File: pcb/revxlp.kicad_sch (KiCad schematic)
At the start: 137 parts, among them Q1 AO3416 N-channel MOSFET, SW1 SW_SPDT, SW2 SW_Push, U1 74HC595, U2 SeeeduinoXIAO_BLE

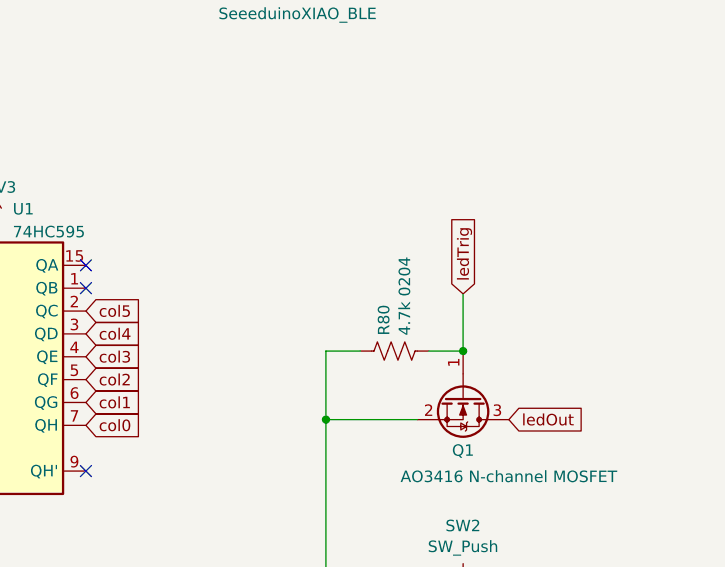
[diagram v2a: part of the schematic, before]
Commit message: Add more LCSC part numbers.
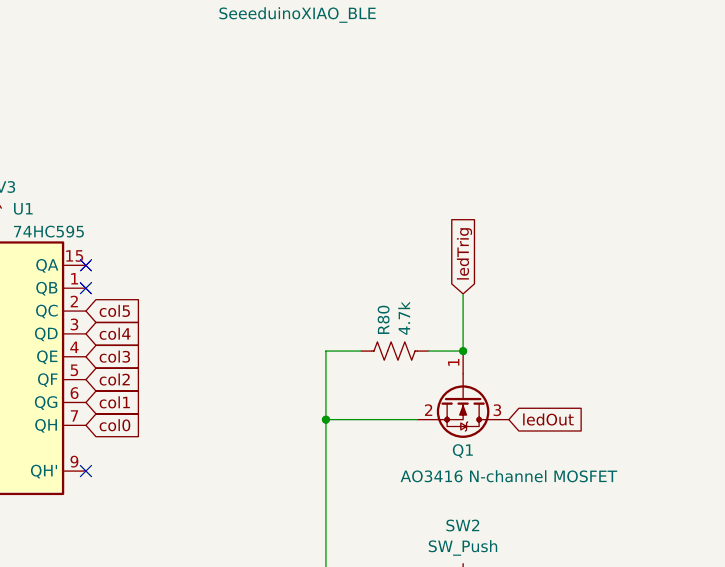
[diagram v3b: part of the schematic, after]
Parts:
- D_A0, D_A1, D_A2, D_A3, D_A4, D_A5, D_B0, D_B1, D_B2, D_B3, D_B4, D_B5, D_C0, D_C1, D_C2, D_C3, D_C4, D_C5, D_D0, D_D1, D_D2, D_D3, D_D4, D_D5, D_E0, D_E1, D_E2, D_E3, D_E4, D_E5, D_F0, D_F1, D_F2, D_F3, D_F4, D_F5, D_G0, D_G1, D_G2, D_G3, D_G4, D_G5: lcsc part number (none) -> C81598
- R80: value 4.7k 0204 -> 4.7k
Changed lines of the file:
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@@
+      (effects (font (size 1.27 1.27)) hide)
+    )
+    (property "lcsc part number" "C81598" (id 4) (at 34.29 39.37 90)
       (effects (font (size 1.27 1.27)) hide)
     )
@@
       (effects (font (size 1.27 1.27)) hide)
     )
+    (property "lcsc part number" "C81598" (id 4) (at 34.29 39.37 90)
+      (effects (font (size 1.27 1.27)) hide)
+    )
     (pin "1")
     (pin "2")
@@
       (effects (font (size 1.27 1.27)) hide)
     )
+    (property "lcsc part number" "C81598" (id 4) (at 34.29 39.37 90)
+      (effects (font (size 1.27 1.27)) hide)
+    )
     (pin "1")
     (pin "2")
@@
       (effects (font (size 1.27 1.27)) hide)
     )
+    (property "lcsc part number" "C81598" (id 4) (at 34.29 39.37 90)
+      (effects (font (size 1.27 1.27)) hide)
+    )
     (pin "1")
     (pin "2")
@@
       (effects (font (size 1.27 1.27)) hide)
     )
+    (property "lcsc part number" "C81598" (id 4) (at 34.29 39.37 90)
+      (effects (font (size 1.27 1.27)) hide)
+    )
     (pin "1")
     (pin "2")
@@
       (effects (font (size 1.27 1.27)) hide)
     )
+    (property "lcsc part number" "C81598" (id 4) (at 34.29 39.37 90)
+      (effects (font (size 1.27 1.27)) hide)
+    )
     (pin "1")
     (pin "2")
@@
       (effects (font (size 1.27 1.27)) hide)
     )
+    (property "lcsc part number" "C81598" (id 4) (at 34.29 39.37 90)
+      (effects (font (size 1.27 1.27)) hide)
+    )
     (pin "1")
     (pin "2")
@@
       (effects (font (size 1.27 1.27)) hide)
     )
+    (property "lcsc part number" "C81598" (id 4) (at 34.29 39.37 90)
+      (effects (font (size 1.27 1.27)) hide)
+    )
     (pin "1")
     (pin "2")
@@
       (effects (font (size 1.27 1.27)) hide)
     )
+    (property "lcsc part number" "C81598" (id 4) (at 34.29 39.37 90)
+      (effects (font (size 1.27 1.27)) hide)
+    )
     (pin "1")
     (pin "2")
@@
       (effects (font (size 1.27 1.27)) hide)
     )
+    (property "lcsc part number" "C81598" (id 4) (at 34.29 39.37 90)
+      (effects (font (size 1.27 1.27)) hide)
+    )
     (pin "1")
     (pin "2")
@@
       (effects (font (size 1.27 1.27)) hide)
     )
+    (property "lcsc part number" "C81598" (id 4) (at 34.29 39.37 90)
+      (effects (font (size 1.27 1.27)) hide)
+    )
     (pin "1")
     (pin "2")
@@
       (effects (font (size 1.27 1.27)) hide)
     )
+    (property "lcsc part number" "C81598" (id 4) (at 34.29 39.37 90)
+      (effects (font (size 1.27 1.27)) hide)
+    )
     (pin "1")
     (pin "2")
@@
       (effects (font (size 1.27 1.27)) hide)
     )
+    (property "lcsc part number" "C81598" (id 4) (at 34.29 39.37 90)
+      (effects (font (size 1.27 1.27)) hide)
+    )
     (pin "1")
     (pin "2")
@@
       (effects (font (size 1.27 1.27)) hide)
     )
+    (property "lcsc part number" "C81598" (id 4) (at 34.29 39.37 90)
+      (effects (font (size 1.27 1.27)) hide)
+    )
     (pin "1")
     (pin "2")
@@
       (effects (font (size 1.27 1.27)) hide)
     )
+    (property "lcsc part number" "C81598" (id 4) (at 34.29 39.37 90)
+      (effects (font (size 1.27 1.27)) hide)
+    )
     (pin "1")
     (pin "2")
@@
       (effects (font (size 1.27 1.27)) hide)
     )
+    (property "lcsc part number" "C81598" (id 4) (at 34.29 39.37 90)
+      (effects (font (size 1.27 1.27)) hide)
+    )
     (pin "1")
     (pin "2")
@@
       (effects (font (size 1.27 1.27)) hide)
     )
+    (property "lcsc part number" "C81598" (id 4) (at 34.29 39.37 90)
+      (effects (font (size 1.27 1.27)) hide)
+    )
     (pin "1")
     (pin "2")
@@
       (effects (font (size 1.27 1.27)) hide)
     )
+    (property "lcsc part number" "C81598" (id 4) (at 34.29 39.37 90)
+      (effects (font (size 1.27 1.27)) hide)
+    )
     (pin "1")
     (pin "2")
@@
       (effects (font (size 1.27 1.27)) hide)
     )
+    (property "lcsc part number" "C81598" (id 4) (at 34.29 39.37 90)
+      (effects (font (size 1.27 1.27)) hide)
+    )
     (pin "1")
     (pin "2")
@@
       (effects (font (size 1.27 1.27)) hide)
     )
+    (property "lcsc part number" "C81598" (id 4) (at 34.29 39.37 90)
+      (effects (font (size 1.27 1.27)) hide)
+    )
     (pin "1")
     (pin "2")
@@
       (effects (font (size 1.27 1.27)) hide)
     )
+    (property "lcsc part number" "C81598" (id 4) (at 34.29 39.37 90)
+      (effects (font (size 1.27 1.27)) hide)
+    )
     (pin "1")
     (pin "2")
@@
       (effects (font (size 1.27 1.27)) hide)
     )
+    (property "lcsc part number" "C81598" (id 4) (at 34.29 39.37 90)
+      (effects (font (size 1.27 1.27)) hide)
+    )
     (pin "1")
     (pin "2")
@@
       (effects (font (size 1.27 1.27)) hide)
     )
+    (property "lcsc part number" "C81598" (id 4) (at 34.29 39.37 90)
+      (effects (font (size 1.27 1.27)) hide)
+    )
     (pin "1")
     (pin "2")
@@
       (effects (font (size 1.27 1.27)) hide)
     )
+    (property "lcsc part number" "C81598" (id 4) (at 34.29 39.37 90)
+      (effects (font (size 1.27 1.27)) hide)
+    )
     (pin "1")
     (pin "2")
@@
       (effects (font (size 1.27 1.27)) hide)
     )
+    (property "lcsc part number" "C81598" (id 4) (at 34.29 39.37 90)
+      (effects (font (size 1.27 1.27)) hide)
+    )
     (pin "1")
     (pin "2")
@@
       (effects (font (size 1.27 1.27)) hide)
     )
+    (property "lcsc part number" "C81598" (id 4) (at 34.29 39.37 90)
+      (effects (font (size 1.27 1.27)) hide)
+    )
     (pin "1")
     (pin "2")
@@
       (effects (font (size 1.27 1.27)) hide)
     )
+    (property "lcsc part number" "C81598" (id 4) (at 34.29 39.37 90)
+      (effects (font (size 1.27 1.27)) hide)
+    )
     (pin "1")
     (pin "2")
@@
       (effects (font (size 1.27 1.27)) hide)
     )
+    (property "lcsc part number" "C81598" (id 4) (at 34.29 39.37 90)
+      (effects (font (size 1.27 1.27)) hide)
+    )
     (pin "1")
     (pin "2")
@@
       (effects (font (size 1.27 1.27)) hide)
     )
+    (property "lcsc part number" "C81598" (id 4) (at 34.29 39.37 90)
+      (effects (font (size 1.27 1.27)) hide)
+    )
     (pin "1")
     (pin "2")
@@
       (effects (font (size 1.27 1.27)) hide)
     )
+    (property "lcsc part number" "C81598" (id 4) (at 34.29 39.37 90)
+      (effects (font (size 1.27 1.27)) hide)
+    )
     (pin "1")
     (pin "2")
@@
       (effects (font (size 1.27 1.27)) hide)
     )
+    (property "lcsc part number" "C81598" (id 4) (at 34.29 39.37 90)
+      (effects (font (size 1.27 1.27)) hide)
+    )
     (pin "1")
     (pin "2")
@@
       (effects (font (size 1.27 1.27)) hide)
     )
+    (property "lcsc part number" "C81598" (id 4) (at 34.29 39.37 90)
+      (effects (font (size 1.27 1.27)) hide)
+    )
     (pin "1")
     (pin "2")
@@
       (effects (font (size 1.27 1.27)) hide)
     )
+    (property "lcsc part number" "C81598" (id 4) (at 34.29 39.37 90)
+      (effects (font (size 1.27 1.27)) hide)
+    )
     (pin "1")
     (pin "2")
@@
       (effects (font (size 1.27 1.27)) hide)
     )
+    (property "lcsc part number" "C81598" (id 4) (at 34.29 39.37 90)
+      (effects (font (size 1.27 1.27)) hide)
+    )
     (pin "1")
     (pin "2")
@@
       (effects (font (size 1.27 1.27)) hide)
     )
+    (property "lcsc part number" "C81598" (id 4) (at 34.29 39.37 90)
+      (effects (font (size 1.27 1.27)) hide)
+    )
     (pin "1")
     (pin "2")
@@
       (effects (font (size 1.27 1.27)) hide)
     )
+    (property "lcsc part number" "C81598" (id 4) (at 34.29 39.37 90)
+      (effects (font (size 1.27 1.27)) hide)
+    )
     (pin "1")
     (pin "2")
@@
       (effects (font (size 1.27 1.27)) hide)
     )
+    (property "lcsc part number" "C81598" (id 4) (at 34.29 39.37 90)
+      (effects (font (size 1.27 1.27)) hide)
+    )
     (pin "1")
     (pin "2")
@@
       (effects (font (size 1.27 1.27)) hide)
     )
+    (property "lcsc part number" "C81598" (id 4) (at 34.29 39.37 90)
+      (effects (font (size 1.27 1.27)) hide)
+    )
     (pin "1")
     (pin "2")
@@
       (effects (font (size 1.27 1.27)) hide)
     )
+    (property "lcsc part number" "C81598" (id 4) (at 34.29 39.37 90)
+      (effects (font (size 1.27 1.27)) hide)
+    )
     (pin "1")
     (pin "2")
@@
       (effects (font (size 1.27 1.27)) hide)
     )
+    (property "lcsc part number" "C81598" (id 4) (at 34.29 39.37 90)
+      (effects (font (size 1.27 1.27)) hide)
+    )
     (pin "1")
     (pin "2")
@@
       (effects (font (size 1.27 1.27)) hide)
     )
+    (property "lcsc part number" "C81598" (id 4) (at 34.29 39.37 90)
+      (effects (font (size 1.27 1.27)) hide)
+    )
     (pin "1")
     (pin "2")
@@
       (effects (font (size 1.27 1.27)) (justify right))
     )
-    (property "Value" "4.7k 0204" (id 1) (at 252.603 108.7628 0)
+    (property "Value" "4.7k" (id 1) (at 252.603 108.7628 0)
       (effects (font (size 1.27 1.27)) (justify right))
     )
@@
       (effects (font (size 1.27 1.27)) hide)
     )
+    (property "lcsc part number" "C81598" (id 4) (at 34.29 39.37 90)
+      (effects (font (size 1.27 1.27)) hide)
+    )
     (pin "1")
     (pin "2")
@@
     )
     (path "/00000000-0000-0000-0000-000060fcc55b"
-      (reference "R80") (unit 1) (value "4.7k 0204") (footprint "Resistor_SMD:R_1206_3216Metric_Pad1.30x1.75mm_HandSolder")
+      (reference "R80") (unit 1) (value "4.7k") (footprint "Resistor_SMD:R_1206_3216Metric_Pad1.30x1.75mm_HandSolder")
     )
     (path "/00000000-0000-0000-0000-000060909042"

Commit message: Part number for JST socket.
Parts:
- BT2: lcsc part number (none) -> C160402
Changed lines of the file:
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@@
+      (effects (font (size 1.27 1.27)) hide)
+    )
+    (property "lcsc part number" "C160402" (id 4) (at 269.24 161.29 90)
       (effects (font (size 1.27 1.27)) hide)
     )
